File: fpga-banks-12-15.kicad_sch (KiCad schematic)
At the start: 1 part

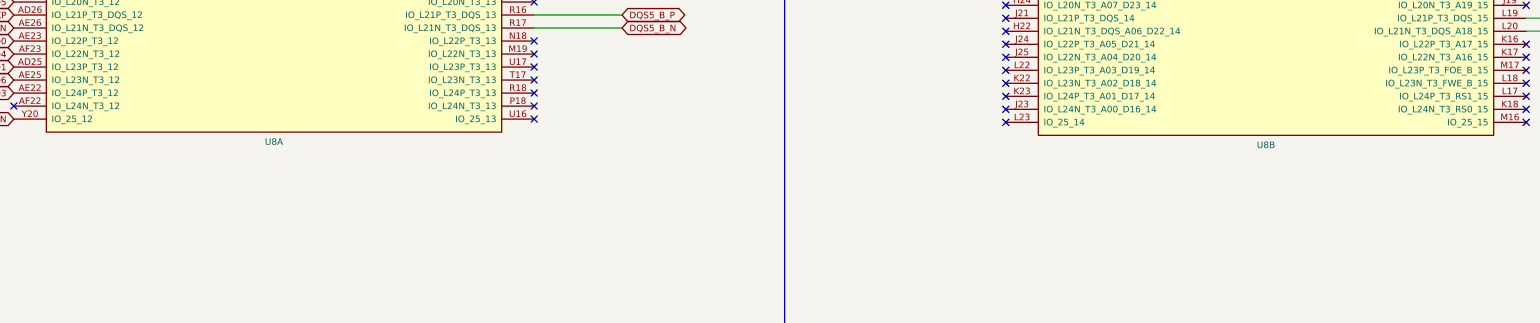
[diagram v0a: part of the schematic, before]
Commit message: Added EN pullup for TPS54561 to avoid disabling by touch
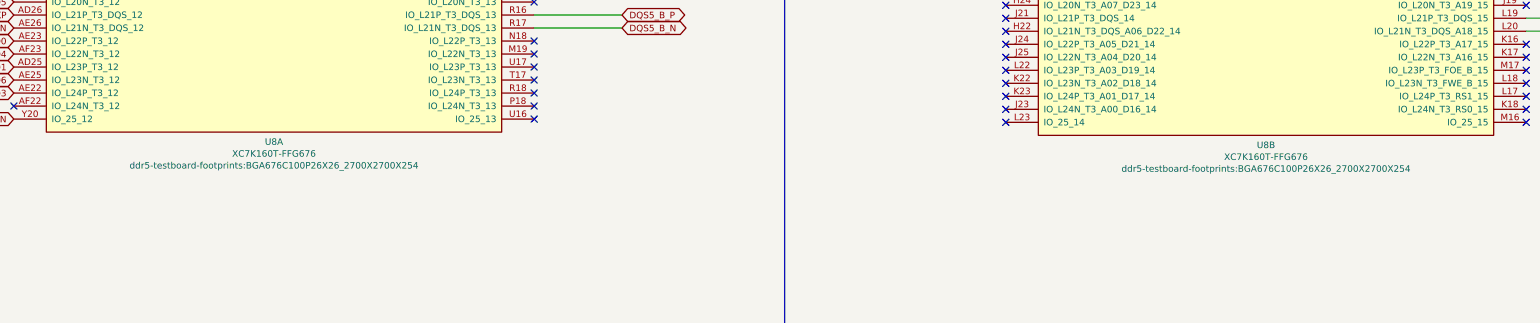
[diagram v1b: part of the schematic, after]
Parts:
- U8: value (none) -> XC7K160T-FFG676; footprint (none) -> ddr5-testboard-footprints:BGA676C100P26X26_2700X2700X254
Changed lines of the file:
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@@
     (in_bom yes) (on_board yes)
     (property "Reference" "U8" (id 0) (at 110.49 220.98 0))
-    (property "Value" "" (id 1) (at 110.49 223.2914 0))
-    (property "Footprint" "" (id 2) (at 110.49 225.6028 0))
+    (property "Value" "XC7K160T-FFG676" (id 1) (at 110.49 223.2914 0))
+    (property "Footprint" "ddr5-testboard-footprints:BGA676C100P26X26_2700X2700X254" (id 2) (at 110.49 225.6028 0))
     (property "Datasheet" "" (id 3) (at 110.49 145.415 0))
     (pin "AA21")
@@
     (in_bom yes) (on_board yes)
     (property "Reference" "U8" (id 0) (at 304.165 221.615 0))
-    (property "Value" "" (id 1) (at 304.165 223.9264 0))
-    (property "Footprint" "" (id 2) (at 304.165 226.2378 0))
+    (property "Value" "XC7K160T-FFG676" (id 1) (at 304.165 223.9264 0))
+    (property "Footprint" "ddr5-testboard-footprints:BGA676C100P26X26_2700X2700X254" (id 2) (at 304.165 226.2378 0))
     (property "Datasheet" "" (id 3) (at 304.165 146.05 0))
     (pin "AA21")

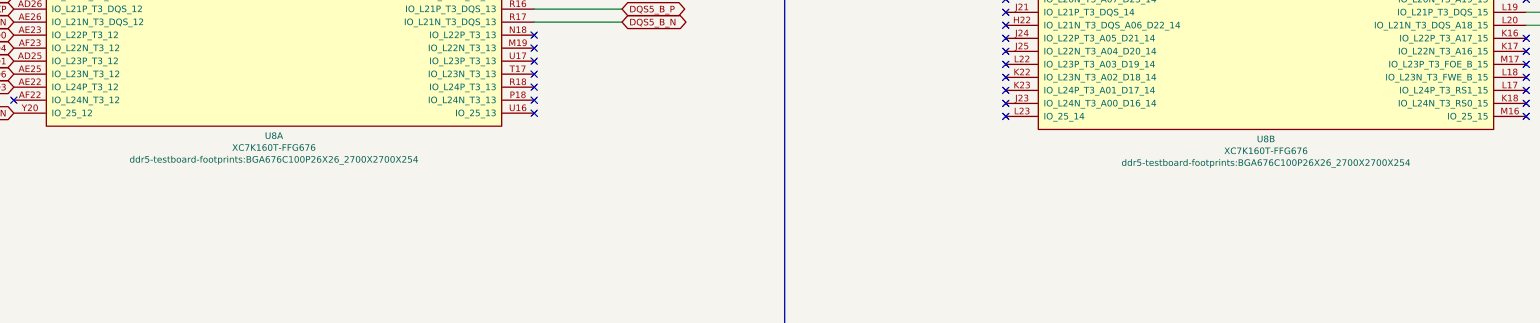
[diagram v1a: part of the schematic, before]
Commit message: Update FPGA footprint reference
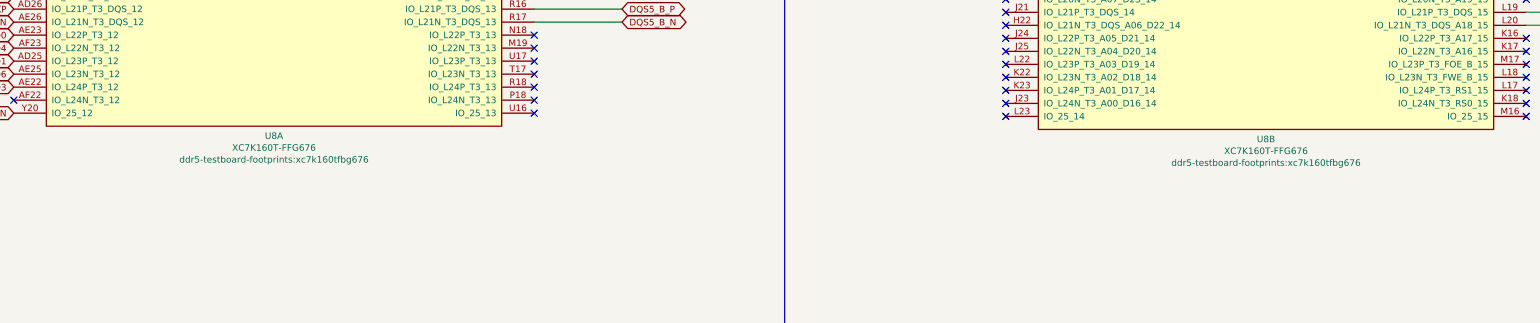
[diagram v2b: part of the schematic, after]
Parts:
- U8: footprint ddr5-testboard-footprints:BGA676C100P26X26_2700X2700X254 -> ddr5-testboard-footprints:xc7k160tfbg676
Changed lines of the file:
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@@
     (property "Reference" "U8" (id 0) (at 110.49 220.98 0))
     (property "Value" "XC7K160T-FFG676" (id 1) (at 110.49 223.2914 0))
-    (property "Footprint" "ddr5-testboard-footprints:BGA676C100P26X26_2700X2700X254" (id 2) (at 110.49 225.6028 0))
+    (property "Footprint" "ddr5-testboard-footprints:xc7k160tfbg676" (id 2) (at 110.49 225.6028 0))
     (property "Datasheet" "" (id 3) (at 110.49 145.415 0))
     (pin "AA21")
@@
     (pin "Y9")
   )
-  (symbol (lib_id "ddr5-testboard:XC7K160T-FFG676") (at 304.165 146.05 0) (unit 2)
+  (symbol (lib_name "XC7K160T-FFG676_1") (lib_id "ddr5-testboard:XC7K160T-FFG676") (at 304.165 146.05 0) (unit 2)
     (in_bom yes) (on_board yes)
     (property "Reference" "U8" (id 0) (at 304.165 221.615 0))
     (property "Value" "XC7K160T-FFG676" (id 1) (at 304.165 223.9264 0))
-    (property "Footprint" "ddr5-testboard-footprints:BGA676C100P26X26_2700X2700X254" (id 2) (at 304.165 226.2378 0))
+    (property "Footprint" "ddr5-testboard-footprints:xc7k160tfbg676" (id 2) (at 304.165 226.2378 0))
     (property "Datasheet" "" (id 3) (at 304.165 146.05 0))
     (pin "AA21")

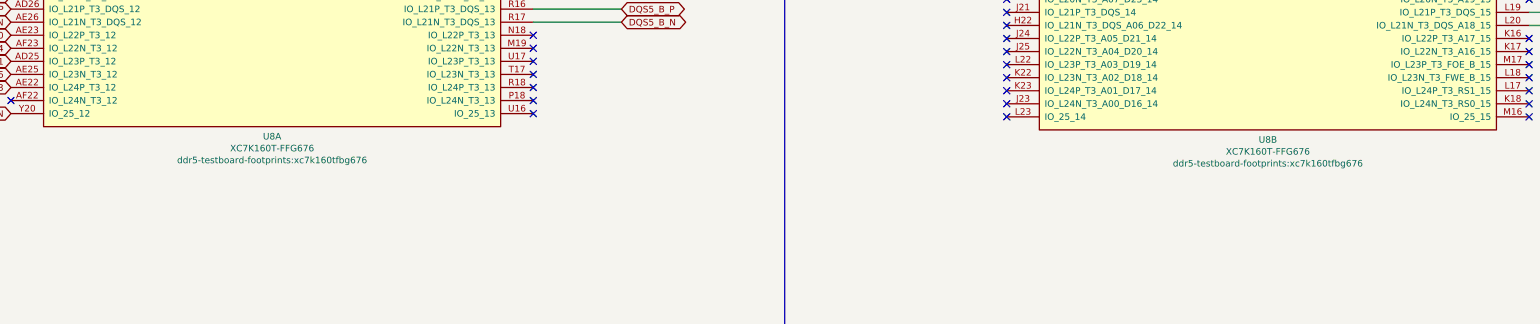
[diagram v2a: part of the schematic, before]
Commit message: Update naming convention
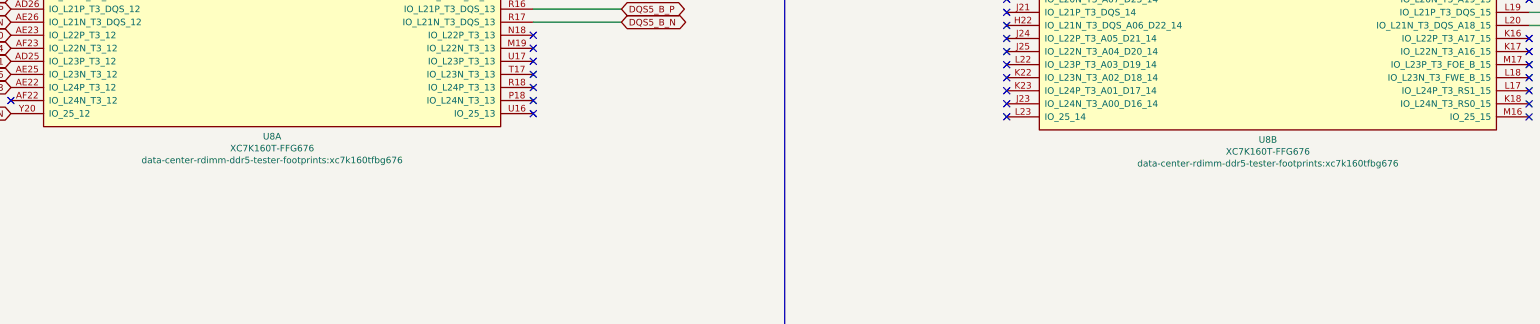
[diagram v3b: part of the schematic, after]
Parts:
- U8: footprint ddr5-testboard-footprints:xc7k160tfbg676 -> data-center-rdimm-ddr5-tester-footprints:xc7k160tfbg676; symbol ddr5-testboard:XC7K160T-FFG676 -> data-center-rdimm-ddr5-tester:XC7K160T-FFG676
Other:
- title: DDR5 Tester -> Data Center RDIMM DDR5 Tester
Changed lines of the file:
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@@
   (paper "A3")
   (title_block
-    (title "DDR5 Tester")
+    (title "Data Center RDIMM DDR5 Tester")
     (date "2022-03-08")
     (rev "1.0.0")
@@
     )
   )
-  (symbol (lib_id "ddr5-testboard:XC7K160T-FFG676") (at 110.49 145.415 0) (unit 1)
+  (symbol (lib_id "data-center-rdimm-ddr5-tester:XC7K160T-FFG676") (at 110.49 145.415 0) (unit 1)
     (in_bom yes) (on_board yes)
     (property "Reference" "U8" (id 0) (at 110.49 220.98 0))
     (property "Value" "XC7K160T-FFG676" (id 1) (at 110.49 223.2914 0))
-    (property "Footprint" "ddr5-testboard-footprints:xc7k160tfbg676" (id 2) (at 110.49 225.6028 0))
+    (property "Footprint" "data-center-rdimm-ddr5-tester-footprints:xc7k160tfbg676" (id 2) (at 110.49 225.6028 0))
     (property "Datasheet" "" (id 3) (at 110.49 145.415 0))
     (pin "AA21")
@@
     (pin "Y9")
   )
-  (symbol (lib_name "XC7K160T-FFG676_1") (lib_id "ddr5-testboard:XC7K160T-FFG676") (at 304.165 146.05 0) (unit 2)
+  (symbol (lib_name "XC7K160T-FFG676_1") (lib_id "data-center-rdimm-ddr5-tester:XC7K160T-FFG676") (at 304.165 146.05 0) (unit 2)
     (in_bom yes) (on_board yes)
     (property "Reference" "U8" (id 0) (at 304.165 221.615 0))
     (property "Value" "XC7K160T-FFG676" (id 1) (at 304.165 223.9264 0))
-    (property "Footprint" "ddr5-testboard-footprints:xc7k160tfbg676" (id 2) (at 304.165 226.2378 0))
+    (property "Footprint" "data-center-rdimm-ddr5-tester-footprints:xc7k160tfbg676" (id 2) (at 304.165 226.2378 0))
     (property "Datasheet" "" (id 3) (at 304.165 146.05 0))
     (pin "AA21")

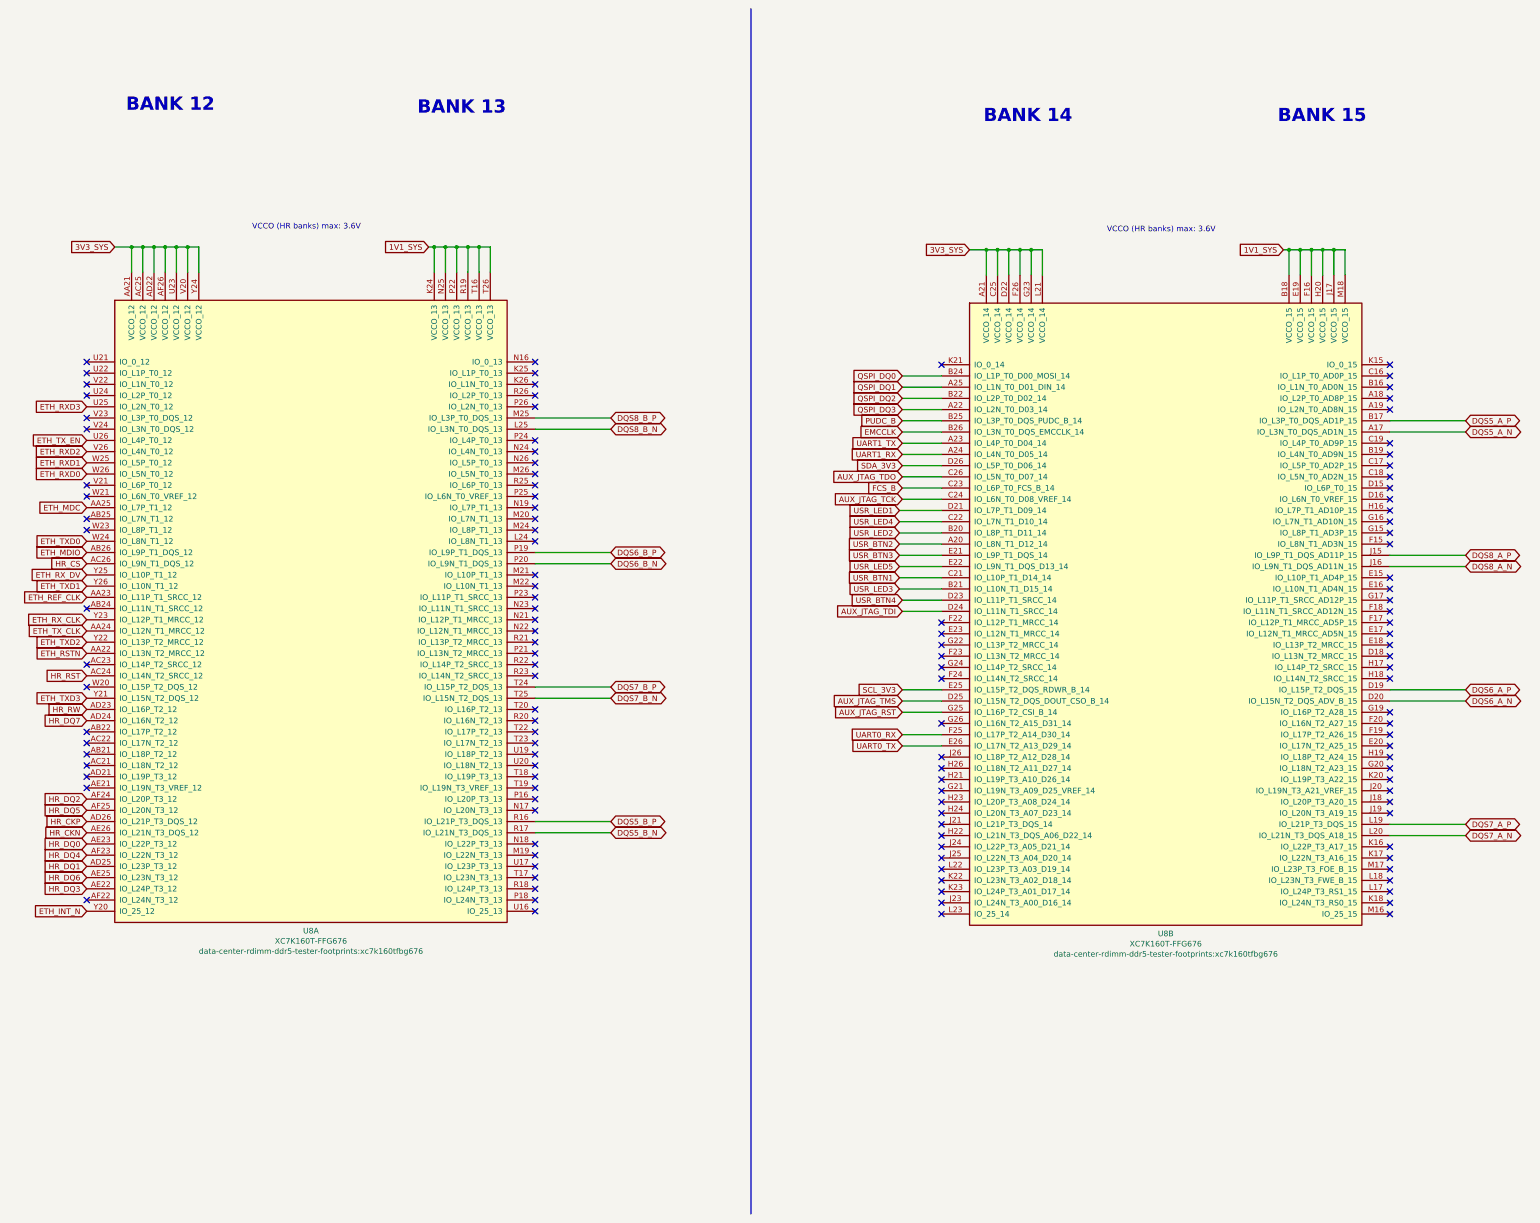
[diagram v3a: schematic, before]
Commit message: Introduce component standarization
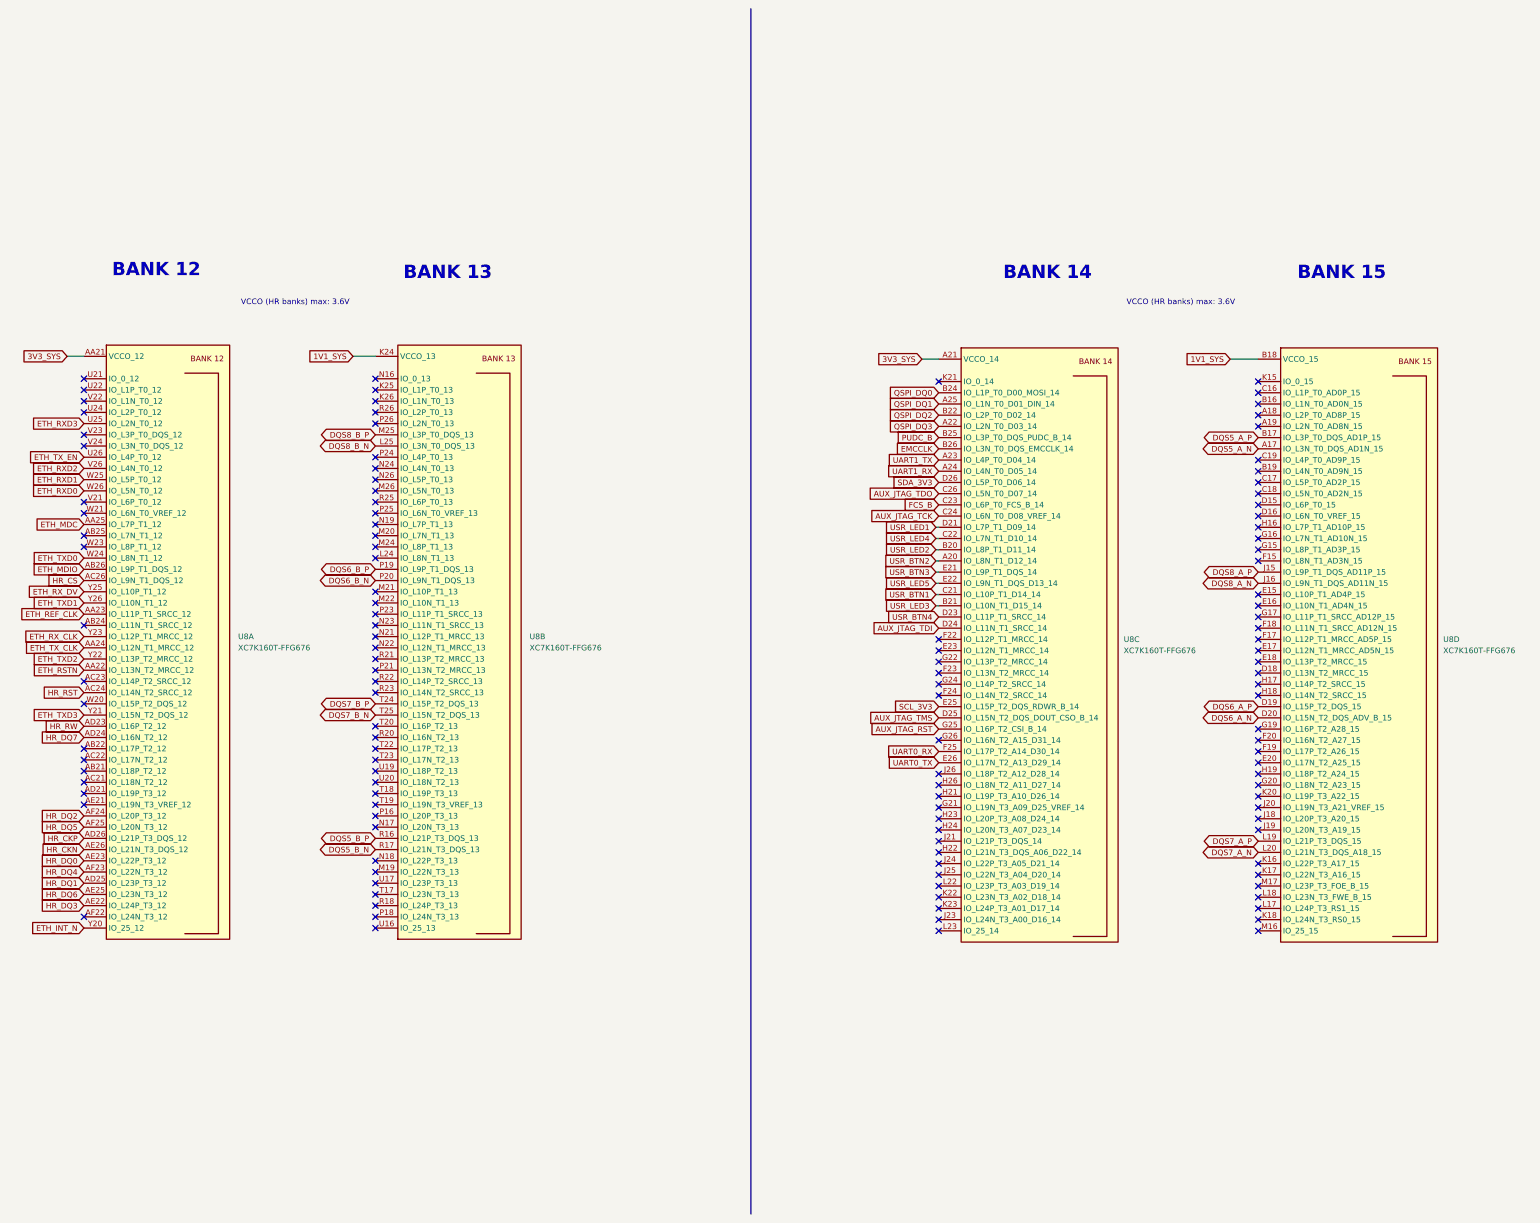
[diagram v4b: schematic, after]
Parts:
- added unit 4 of U8
- added unit 2 of U8
- U8: footprint data-center-rdimm-ddr5-tester-footprints:xc7k160tfbg676 -> data-center-rdimm-ddr5-tester-footprints:BGA-676_27x27mm_Layout26x26_P1X1mm; Author (none) -> Antmicro; License (none) -> Apache-2.0; MPN (none) -> XC7K160T-FFG676; Manufacturer (none) -> Xilinx
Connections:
- net 1V1_SYS: now also U8.B18 (VCCO_15), U8.E19 (VCCO_15), U8.F16 (VCCO_15), U8.H20 (VCCO_15), U8.J17 (VCCO_15), U8.K24 (VCCO_13), U8.M18 (VCCO_15), U8.N25 (VCCO_13), U8.P22 (VCCO_13), U8.R19 (VCCO_13), U8.T16 (VCCO_13), U8.T26 (VCCO_13); no longer U8.B18 (VCCO_15), U8.E19 (VCCO_15), U8.F16 (VCCO_15), U8.H20 (VCCO_15), U8.J17 (VCCO_15), U8.K24 (VCCO_13), U8.M18 (VCCO_15), U8.N25 (VCCO_13), U8.P22 (VCCO_13), U8.R19 (VCCO_13), U8.T16 (VCCO_13), U8.T26 (VCCO_13)
- net DQS5_A_N: now also U8.A17 (IO_L3N_T0_DQS_AD1N_15); no longer U8.A17 (IO_L3N_T0_DQS_AD1N_15)
- net DQS5_A_P: now also U8.B17 (IO_L3P_T0_DQS_AD1P_15); no longer U8.B17 (IO_L3P_T0_DQS_AD1P_15)
- net DQS5_B_N: now also U8.R17 (IO_L21N_T3_DQS_13); no longer U8.R17 (IO_L21N_T3_DQS_13)
- net DQS5_B_P: now also U8.R16 (IO_L21P_T3_DQS_13); no longer U8.R16 (IO_L21P_T3_DQS_13)
- net DQS6_A_N: now also U8.D20 (IO_L15N_T2_DQS_ADV_B_15); no longer U8.D20 (IO_L15N_T2_DQS_ADV_B_15)
- net DQS6_A_P: now also U8.D19 (IO_L15P_T2_DQS_15); no longer U8.D19 (IO_L15P_T2_DQS_15)
- net DQS6_B_N: now also U8.P20 (IO_L9N_T1_DQS_13); no longer U8.P20 (IO_L9N_T1_DQS_13)
- net DQS6_B_P: now also U8.P19 (IO_L9P_T1_DQS_13); no longer U8.P19 (IO_L9P_T1_DQS_13)
- net DQS7_A_N: now also U8.L20 (IO_L21N_T3_DQS_A18_15); no longer U8.L20 (IO_L21N_T3_DQS_A18_15)
- net DQS7_A_P: now also U8.L19 (IO_L21P_T3_DQS_15); no longer U8.L19 (IO_L21P_T3_DQS_15)
- net DQS7_B_N: now also U8.T25 (IO_L15N_T2_DQS_13); no longer U8.T25 (IO_L15N_T2_DQS_13)
- net DQS7_B_P: now also U8.T24 (IO_L15P_T2_DQS_13); no longer U8.T24 (IO_L15P_T2_DQS_13)
- net DQS8_A_N: now also U8.J16 (IO_L9N_T1_DQS_AD11N_15); no longer U8.J16 (IO_L9N_T1_DQS_AD11N_15)
- net DQS8_A_P: now also U8.J15 (IO_L9P_T1_DQS_AD11P_15); no longer U8.J15 (IO_L9P_T1_DQS_AD11P_15)
- net DQS8_B_N: now also U8.L25 (IO_L3N_T0_DQS_13); no longer U8.L25 (IO_L3N_T0_DQS_13)
- net DQS8_B_P: now also U8.M25 (IO_L3P_T0_DQS_13); no longer U8.M25 (IO_L3P_T0_DQS_13)

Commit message: [#55296] component update
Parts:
- U8: Manufacturer Xilinx -> AMD-Xilinx
